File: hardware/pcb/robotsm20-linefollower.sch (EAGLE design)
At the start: 75 parts, among them IC2 TPS43061RTER, Q1 CSD15571Q2, Q2 CSD15571Q2, U1 STM32F405RG

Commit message: Debug + UART connector and OLED Screen
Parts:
- added DEBUG_CONNECTOR, UART_CONNECTOR: JST-EH-03, CASE-JST:EH_B3B-EH
- added U$6: DISPLAY-OLED-128X64-I2C, Displays:DISPLAY-OLED-128X64-I2C
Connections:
- new net N$28: U$6.VCC
- net GND: now also DEBUG_CONNECTOR.3, U$6.GND, UART_CONNECTOR.3
- net RX_HEADER: now also UART_CONNECTOR.1
- net SCL: now also U$6.SCL
- net SDA: now also U$6.SDA
- net SWCLK: now also DEBUG_CONNECTOR.1
- net SWDIO: now also DEBUG_CONNECTOR.2
- net TX_HEADER: now also UART_CONNECTOR.2
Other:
- note removed: "- Debug header (SWD)"
- note removed: "BOOT MODE"
- note removed: "TODO"

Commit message: Update
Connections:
- removed net N$28: U$6.VCC
- net +5V: now also U$6.VCC
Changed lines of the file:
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@@
 <schematic_group name="BOOT_MODE"/>
 <schematic_group name="RESET_BUTTON"/>
+<schematic_group name="OLED"/>
 </groups>
 <parts>
@@
 <part name="U$6" library="Displays" library_urn="urn:adsk.eagle:library:17801130" deviceset="DISPLAY-OLED-128X64-I2C" device="" package3d_urn="urn:adsk.eagle:package:17801164/1"/>
 <part name="SUPPLY57" library="supply2" library_urn="urn:adsk.eagle:library:372" deviceset="GND" device=""/>
+<part name="P+7" library="supply1" library_urn="urn:adsk.eagle:library:371" deviceset="+5V" device=""/>
 </parts>
 <sheets>
@@
 <attribute name="SHEET" x="207.645" y="-111.76" size="2.54" layer="94"/>
 </instance>
-<instance part="U$6" gate="G$1" x="-93.98" y="88.9" smashed="yes">
+<instance part="U$6" gate="G$1" x="-93.98" y="88.9" smashed="yes" grouprefs="OLED">
 <attribute name="NAME" x="-111.76" y="68.58" size="1.778" layer="95"/>
 <attribute name="VALUE" x="-111.76" y="71.12" size="1.778" layer="96"/>
 </instance>
-<instance part="SUPPLY57" gate="GND" x="-106.68" y="114.3" smashed="yes">
+<instance part="SUPPLY57" gate="GND" x="-106.68" y="114.3" smashed="yes" grouprefs="OLED">
 <attribute name="VALUE" x="-108.585" y="111.125" size="1.778" layer="96"/>
+</instance>
+<instance part="P+7" gate="1" x="-96.52" y="127" smashed="yes" grouprefs="OLED">
+<attribute name="VALUE" x="-99.06" y="121.92" size="1.778" layer="96" rot="R90"/>
 </instance>
 </instances>
@@
 <segment>
 <pinref part="U$6" gate="G$1" pin="GND"/>
-<wire x1="-99.06" y1="109.22" x2="-99.06" y2="119.38" width="0.1524" layer="91"/>
-<wire x1="-99.06" y1="119.38" x2="-106.68" y2="119.38" width="0.1524" layer="91"/>
-<wire x1="-106.68" y1="119.38" x2="-106.68" y2="116.84" width="0.1524" layer="91"/>
+<wire x1="-99.06" y1="109.22" x2="-99.06" y2="119.38" width="0.1524" layer="91" grouprefs="OLED"/>
+<wire x1="-99.06" y1="119.38" x2="-106.68" y2="119.38" width="0.1524" layer="91" grouprefs="OLED"/>
+<wire x1="-106.68" y1="119.38" x2="-106.68" y2="116.84" width="0.1524" layer="91" grouprefs="OLED"/>
 <pinref part="SUPPLY57" gate="GND" pin="GND"/>
 </segment>
 </net>
-<net name="N$28" class="0">
+<net name="+5V" class="0">
 <segment>
 <pinref part="U$6" gate="G$1" pin="VCC"/>
-<wire x1="-96.52" y1="109.22" x2="-96.52" y2="124.46" width="0.1524" layer="91"/>
+<wire x1="-96.52" y1="109.22" x2="-96.52" y2="124.46" width="0.1524" layer="91" grouprefs="OLED"/>
+<pinref part="P+7" gate="1" pin="+5V"/>
 </segment>
 </net>
@@
 <segment>
 <pinref part="U$6" gate="G$1" pin="SCL"/>
-<wire x1="-93.98" y1="109.22" x2="-93.98" y2="121.92" width="0.1524" layer="91"/>
-<wire x1="-93.98" y1="121.92" x2="-83.82" y2="121.92" width="0.1524" layer="91"/>
-<label x="-88.9" y="121.92" size="1.778" layer="95"/>
+<wire x1="-93.98" y1="109.22" x2="-93.98" y2="121.92" width="0.1524" layer="91" grouprefs="OLED"/>
+<wire x1="-93.98" y1="121.92" x2="-83.82" y2="121.92" width="0.1524" layer="91" grouprefs="OLED"/>
+<label x="-88.9" y="121.92" size="1.778" layer="95" grouprefs="OLED"/>
 </segment>
 </net>
@@
 <segment>
 <pinref part="U$6" gate="G$1" pin="SDA"/>
-<wire x1="-91.44" y1="109.22" x2="-91.44" y2="119.38" width="0.1524" layer="91"/>
-<wire x1="-91.44" y1="119.38" x2="-83.82" y2="119.38" width="0.1524" layer="91"/>
-<label x="-88.9" y="119.38" size="1.778" layer="95"/>
-</segment>
-</net>
+<wire x1="-91.44" y1="109.22" x2="-91.44" y2="119.38" width="0.1524" layer="91" grouprefs="OLED"/>
+<wire x1="-91.44" y1="119.38" x2="-83.82" y2="119.38" width="0.1524" layer="91" grouprefs="OLED"/>
+<label x="-88.9" y="119.38" size="1.778" layer="95" grouprefs="OLED"/>
+</segment>
+</net>

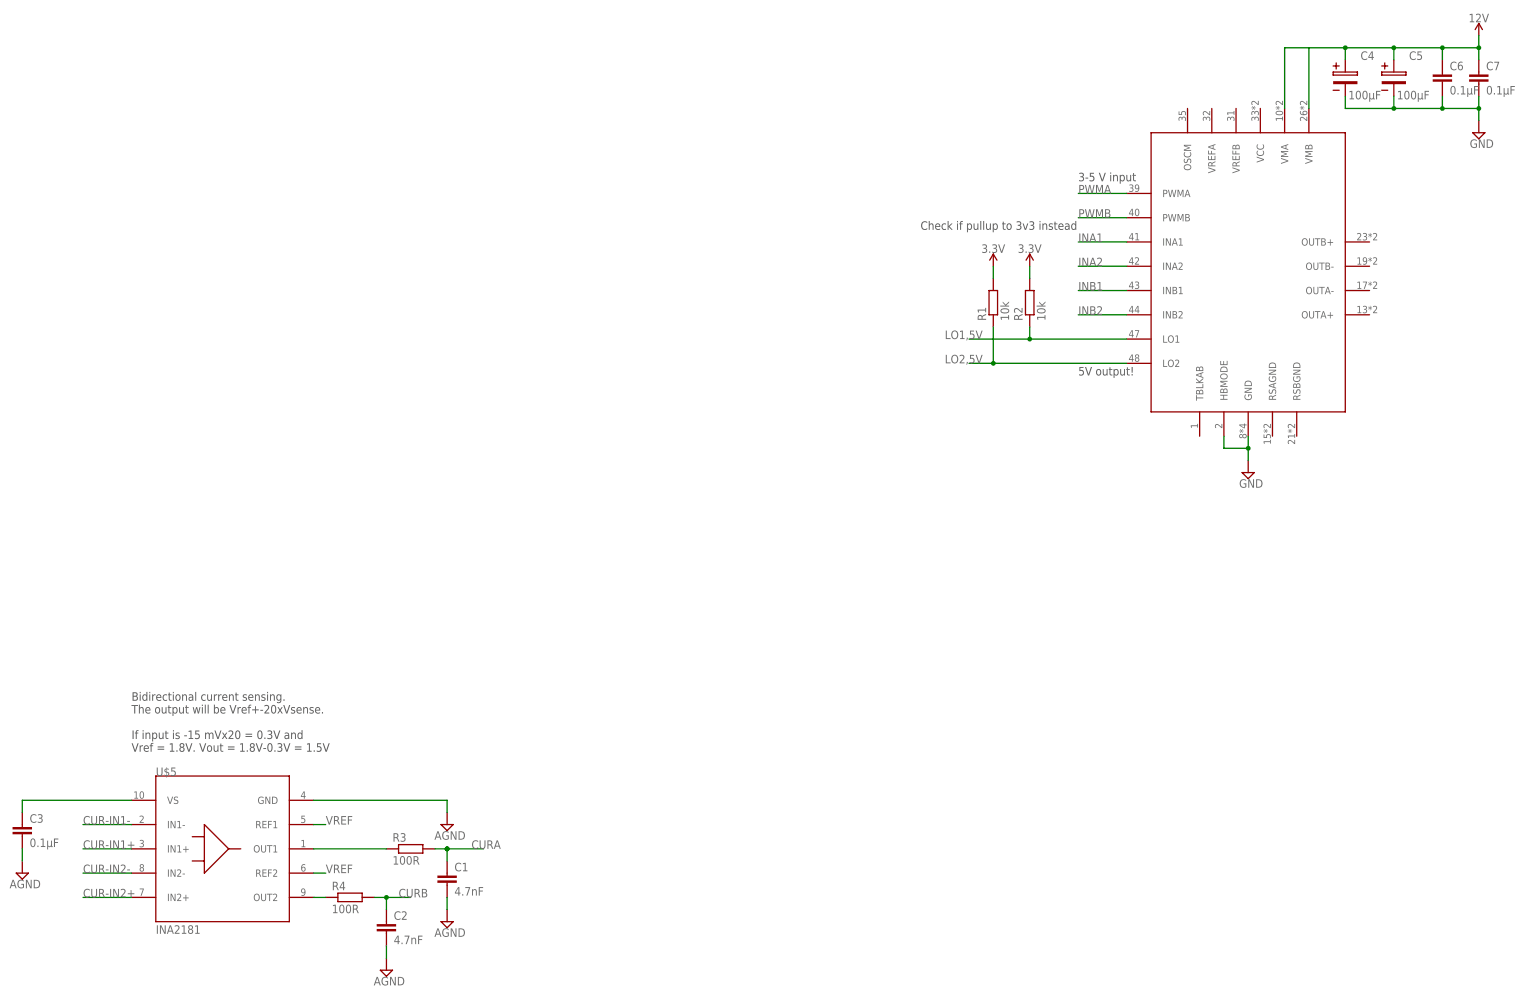
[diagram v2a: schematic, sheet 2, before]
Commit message: Motor driver finished except for ROSC
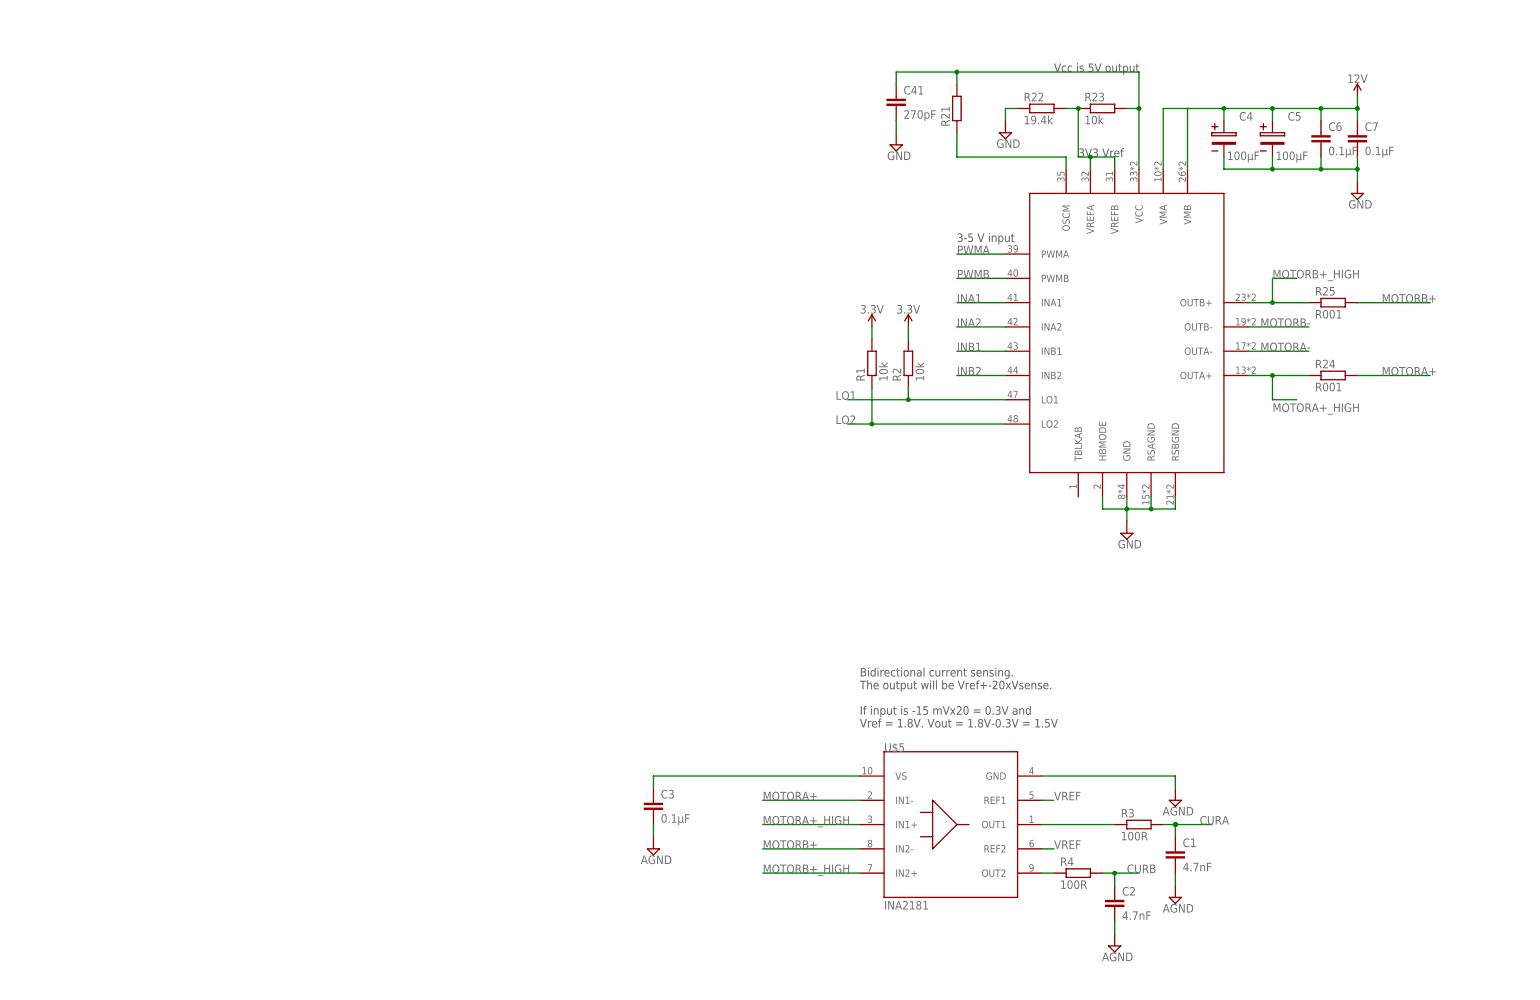
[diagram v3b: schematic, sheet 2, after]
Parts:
- added C41: 270pF, rcl:C-EUC0805
- added R21: (no value), rcl:R-EU_R0603
- added R22: 19.4k, rcl:R-EU_R0603
- added R23: 10k, rcl:R-EU_R0603
- added R24, R25: R001, rcl:R-EU_R2512W
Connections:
- net LO1,5V renamed LO1
- net LO2,5V renamed LO2
- removed net CUR-IN1+: U$5.IN1+
- removed net CUR-IN1-: U$5.IN1-
- removed net CUR-IN2+: U$5.IN2+
- removed net CUR-IN2-: U$5.IN2-
- new net MOTORA+: R24.2, U$5.IN1-
- new net MOTORA+_HIGH: R24.1, U$1.OUTA+, U$5.IN1+
- new net MOTORA-: U$1.OUTA-
- new net MOTORB+: R25.2, U$5.IN2-
- new net MOTORB+_HIGH: R25.1, U$1.OUTB+, U$5.IN2+
- new net MOTORB-: U$1.OUTB-
- new net N$28: R22.2, R23.1, U$1.VREFA, U$1.VREFB
- new net N$29: C41.1, R21.2, R23.2, U$1.VCC
- new net N$31: R21.1, U$1.OSCM
- net GND: now also C41.2, R22.1, U$1.RSAGND, U$1.RSBGND
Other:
- note added: "3V3 Vref"
- note added: "Vcc is 5V output"
- note removed: "5V output!"
- note removed: "Check if pullup to 3v3 instead"
- moved on the sheet: C1, C2, C3, C4, C5, C6, C7, R1, R2, R3, R4, U$5

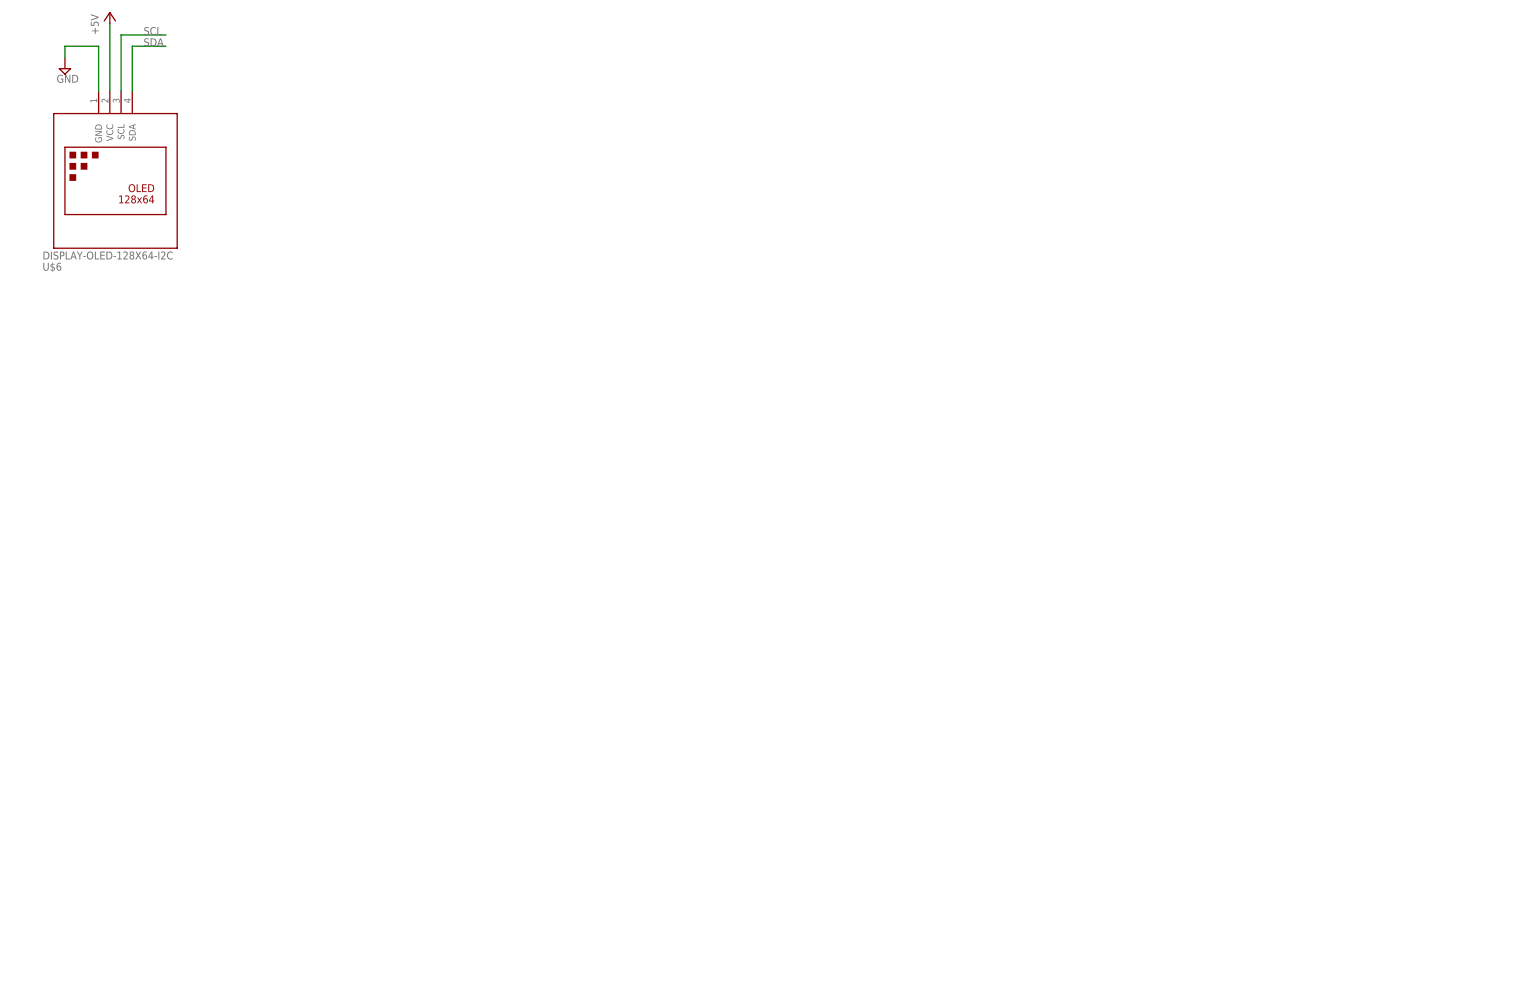
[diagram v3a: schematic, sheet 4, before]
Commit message: Added IMU, Battery switch, BT,
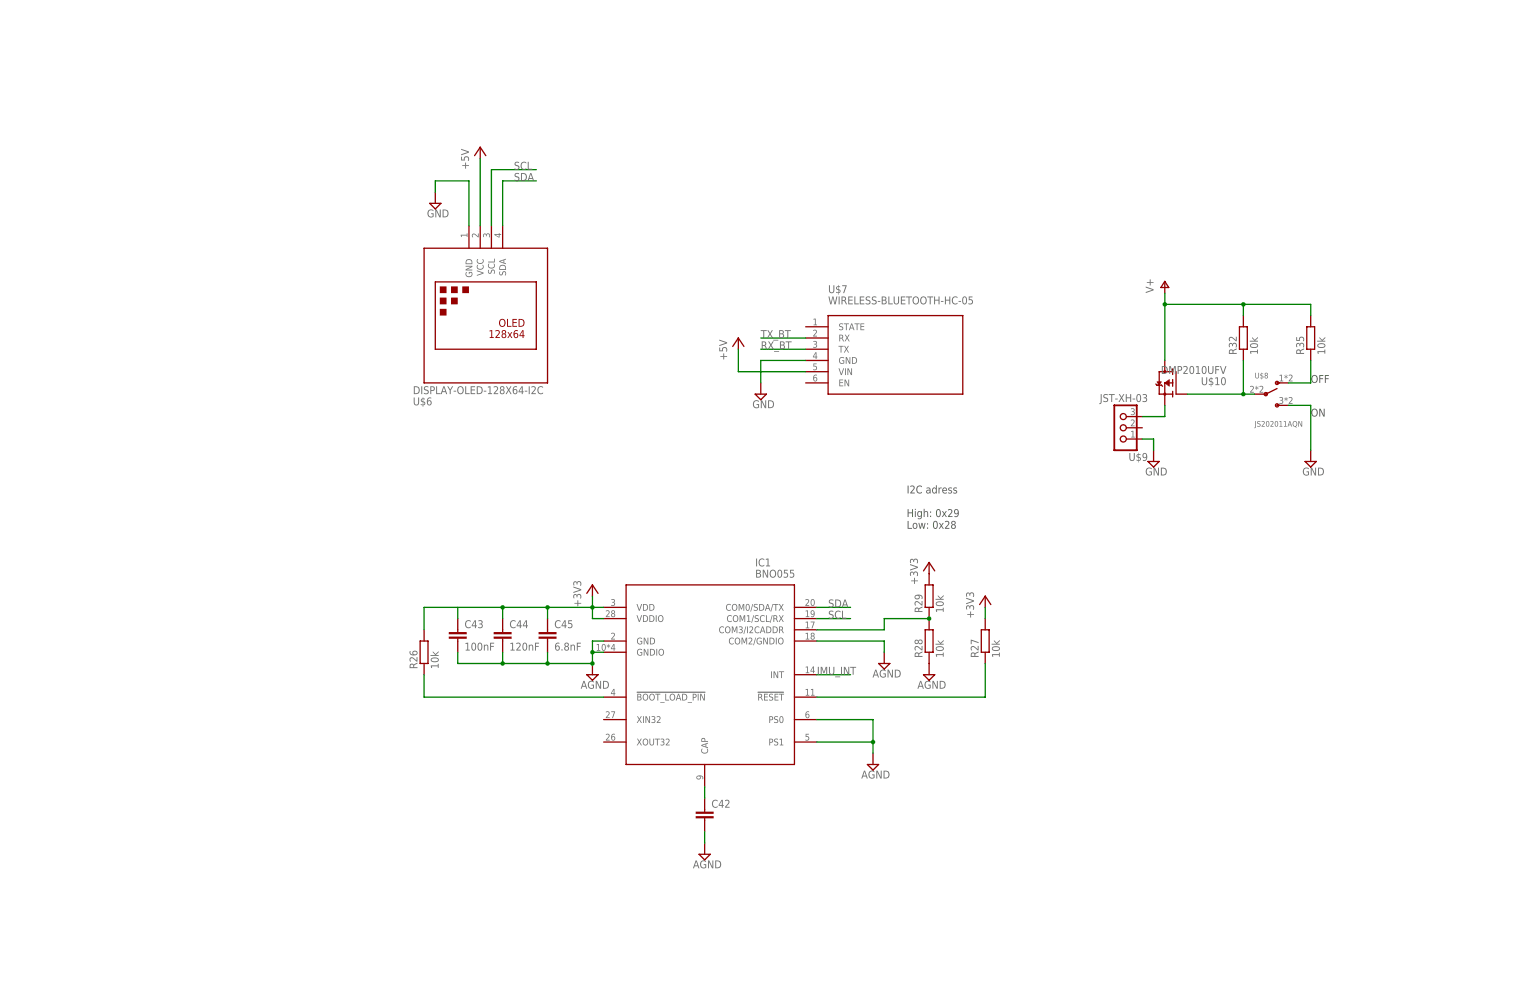
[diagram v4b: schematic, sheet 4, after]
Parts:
- added C42: (no value), rcl:C-EUC0805
- added C43: 100nF, rcl:C-EUC0805
- added C44: 120nF, rcl:C-EUC0805
- added C45: 6.8nF, rcl:C-EUC0805
- added IC1: BNO055, Sensors:BNO055
- added R26, R27, R28, R29, R30, R31, R32, R35: 10k, rcl:R-EU_R0603
- added U$10: DMP2010UFV, PowerManagement:DMP2010UFV
- added U$7: WIRELESS-BLUETOOTH-HC-05, Isaks Bibliotek:WIRELESS-BLUETOOTH-HC-05
- added U$8: JS202011AQN, Switches:JS202011AQN
- added U$9: JST-XH-03, Isaks Bibliotek:JST-XH-03
- R17, R18, R19, R20: value 10k -> (none)
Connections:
- new net IMU_INT: IC1.INT
- new net N$27: IC1.!RESET!, R27.1
- new net N$30: C42.1, IC1.CAP
- new net N$36: C43.1
- new net N$37: IC1.!BOOT_LOAD_PIN!, R26.1
- new net N$38: U$10.S, U$9.3
- new net N$39: IC1.COM3/I2CADDR, R28.2, R29.1
- new net N$40: R32.1, U$10.G, U$8.COM
- new net N$42: R35.1, U$8.NC
- net +3V3: now also C44.1, C45.1, IC1.VDD, IC1.VDDIO, R26.2, R27.2, R29.2
- net +5V: now also U$7.VIN
- net 3.3V: now also R30.1, R31.1
- net AGND: now also C42.2, C43.2, C44.2, C45.2, IC1.COM2/GNDIO, IC1.GND, IC1.GNDIO, IC1.PS0, IC1.PS1, R28.1
- net GND: now also U$7.GND, U$8.NO, U$9.1
- net RX_BT: now also U$7.TX
- net SCL: now also IC1.COM1/SCL/RX, R31.2
- net SDA: now also IC1.COM0/SDA/TX, R30.2
- net TX_BT: now also U$7.RX
- net V+: now also R32.2, R35.2, U$10.D
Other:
- note added: "I2C adress High: 0x29 Low: 0x28"
- note added: "OFF"
- note added: "ON"
- moved on the sheet: C1, C2, C3, R3, R4, U$5, U$6
